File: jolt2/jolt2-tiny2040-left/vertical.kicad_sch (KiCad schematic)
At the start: 4 parts, among them J14 Conn_01x02_Pin, J15 Conn_01x02_Pin, J16 Conn_01x02_Pin, J17 Conn_01x02_Pin

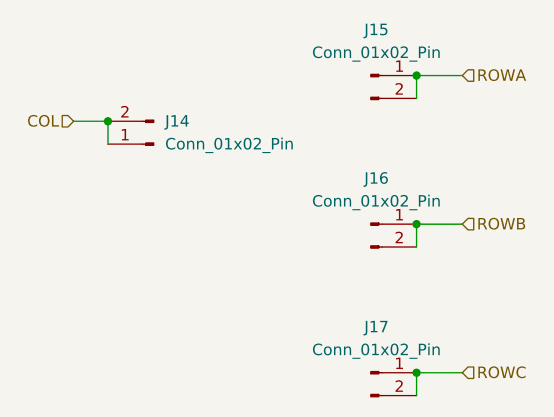
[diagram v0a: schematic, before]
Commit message: jolt2-tiny204-left: Cleanup and route
Fix the designators for all of the pin headers.  This was mostly done
manually, naming them consistently for each component.

Perform manual routing.

This should be ready for REV A.
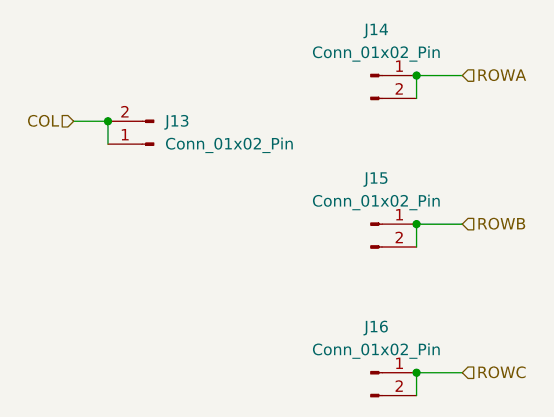
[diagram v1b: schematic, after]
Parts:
- renumbered J14 to J13, J15 to J14, J16 to J15, J17 to J16
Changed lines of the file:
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@@
 		(dnp no)
 		(fields_autoplaced yes)
-		(property "Reference" "J16"
+		(property "Reference" "J15"
 			(at 60.325 63.5 0)
 			(effects
@@
 			(project ""
 				(path "/5e404b8e-7f18-4204-bb67-87c83d2db771/029d86d1-e5b3-4172-a8dd-479e089a0442"
-					(reference "J16")
+					(reference "J15")
 					(unit 1)
 				)
 				(path "/5e404b8e-7f18-4204-bb67-87c83d2db771/17b916f7-ebfc-4d6b-a00a-a1c2400a1083"
-					(reference "J4")
+					(reference "J3")
 					(unit 1)
 				)
 				(path "/5e404b8e-7f18-4204-bb67-87c83d2db771/3ff70a16-bd04-4e60-bc61-4e3e1bf429cd"
-					(reference "J8")
+					(reference "J7")
 					(unit 1)
 				)
 				(path "/5e404b8e-7f18-4204-bb67-87c83d2db771/42146c1c-342d-4727-8b3f-2f54e7f84a3f"
-					(reference "J12")
+					(reference "J11")
 					(unit 1)
 				)
 				(path "/5e404b8e-7f18-4204-bb67-87c83d2db771/c6e71873-f81a-4892-a219-f7518ad6cce9"
-					(reference "J24")
+					(reference "J23")
 					(unit 1)
 				)
 				(path "/5e404b8e-7f18-4204-bb67-87c83d2db771/db596c9f-6bee-4ab9-b1c0-0cb65b9b558f"
-					(reference "J20")
+					(reference "J19")
 					(unit 1)
 				)
 				(path "/5e404b8e-7f18-4204-bb67-87c83d2db771/e95bee69-4f13-400e-8392-2bce6da6b398"
-					(reference "J28")
+					(reference "J27")
 					(unit 1)
 				)
@@
 		(dnp no)
 		(fields_autoplaced yes)
-		(property "Reference" "J15"
+		(property "Reference" "J14"
 			(at 60.325 46.99 0)
 			(effects
@@
 			(project ""
 				(path "/5e404b8e-7f18-4204-bb67-87c83d2db771/029d86d1-e5b3-4172-a8dd-479e089a0442"
-					(reference "J15")
+					(reference "J14")
 					(unit 1)
 				)
 				(path "/5e404b8e-7f18-4204-bb67-87c83d2db771/17b916f7-ebfc-4d6b-a00a-a1c2400a1083"
-					(reference "J3")
+					(reference "J2")
 					(unit 1)
 				)
 				(path "/5e404b8e-7f18-4204-bb67-87c83d2db771/3ff70a16-bd04-4e60-bc61-4e3e1bf429cd"
-					(reference "J7")
+					(reference "J6")
 					(unit 1)
 				)
 				(path "/5e404b8e-7f18-4204-bb67-87c83d2db771/42146c1c-342d-4727-8b3f-2f54e7f84a3f"
-					(reference "J11")
+					(reference "J10")
 					(unit 1)
 				)
 				(path "/5e404b8e-7f18-4204-bb67-87c83d2db771/c6e71873-f81a-4892-a219-f7518ad6cce9"
-					(reference "J23")
+					(reference "J22")
 					(unit 1)
 				)
 				(path "/5e404b8e-7f18-4204-bb67-87c83d2db771/db596c9f-6bee-4ab9-b1c0-0cb65b9b558f"
-					(reference "J19")
+					(reference "J18")
 					(unit 1)
 				)
 				(path "/5e404b8e-7f18-4204-bb67-87c83d2db771/e95bee69-4f13-400e-8392-2bce6da6b398"
-					(reference "J27")
+					(reference "J26")
 					(unit 1)
 				)
@@
 		(dnp no)
 		(fields_autoplaced yes)
-		(property "Reference" "J17"
+		(property "Reference" "J16"
 			(at 60.325 80.01 0)
 			(effects
@@
 			(project ""
 				(path "/5e404b8e-7f18-4204-bb67-87c83d2db771/029d86d1-e5b3-4172-a8dd-479e089a0442"
-					(reference "J17")
+					(reference "J16")
 					(unit 1)
 				)
 				(path "/5e404b8e-7f18-4204-bb67-87c83d2db771/17b916f7-ebfc-4d6b-a00a-a1c2400a1083"
-					(reference "J5")
+					(reference "J4")
 					(unit 1)
 				)
 				(path "/5e404b8e-7f18-4204-bb67-87c83d2db771/3ff70a16-bd04-4e60-bc61-4e3e1bf429cd"
-					(reference "J9")
+					(reference "J8")
 					(unit 1)
 				)
 				(path "/5e404b8e-7f18-4204-bb67-87c83d2db771/42146c1c-342d-4727-8b3f-2f54e7f84a3f"
-					(reference "J13")
+					(reference "J12")
 					(unit 1)
 				)
 				(path "/5e404b8e-7f18-4204-bb67-87c83d2db771/c6e71873-f81a-4892-a219-f7518ad6cce9"
-					(reference "J25")
+					(reference "J24")
 					(unit 1)
 				)
 				(path "/5e404b8e-7f18-4204-bb67-87c83d2db771/db596c9f-6bee-4ab9-b1c0-0cb65b9b558f"
-					(reference "J21")
+					(reference "J20")
 					(unit 1)
 				)
 				(path "/5e404b8e-7f18-4204-bb67-87c83d2db771/e95bee69-4f13-400e-8392-2bce6da6b398"
-					(reference "J29")
+					(reference "J28")
 					(unit 1)
 				)
@@
 		(dnp no)
 		(fields_autoplaced yes)
-		(property "Reference" "J14"
+		(property "Reference" "J13"
 			(at 36.83 57.1499 0)
 			(effects
@@
 			(project ""
 				(path "/5e404b8e-7f18-4204-bb67-87c83d2db771/029d86d1-e5b3-4172-a8dd-479e089a0442"
-					(reference "J14")
+					(reference "J13")
 					(unit 1)
 				)
 				(path "/5e404b8e-7f18-4204-bb67-87c83d2db771/17b916f7-ebfc-4d6b-a00a-a1c2400a1083"
-					(reference "J2")
+					(reference "J1")
 					(unit 1)
 				)
 				(path "/5e404b8e-7f18-4204-bb67-87c83d2db771/3ff70a16-bd04-4e60-bc61-4e3e1bf429cd"
-					(reference "J6")
+					(reference "J5")
 					(unit 1)
 				)
 				(path "/5e404b8e-7f18-4204-bb67-87c83d2db771/42146c1c-342d-4727-8b3f-2f54e7f84a3f"
-					(reference "J10")
+					(reference "J9")
 					(unit 1)
 				)
 				(path "/5e404b8e-7f18-4204-bb67-87c83d2db771/c6e71873-f81a-4892-a219-f7518ad6cce9"
-					(reference "J22")
+					(reference "J21")
 					(unit 1)
 				)
 				(path "/5e404b8e-7f18-4204-bb67-87c83d2db771/db596c9f-6bee-4ab9-b1c0-0cb65b9b558f"
-					(reference "J18")
+					(reference "J17")
 					(unit 1)
 				)
 				(path "/5e404b8e-7f18-4204-bb67-87c83d2db771/e95bee69-4f13-400e-8392-2bce6da6b398"
-					(reference "J26")
-					(unit 1)
-				)
+					(reference "J25")
+					(unit 1)
+				)
